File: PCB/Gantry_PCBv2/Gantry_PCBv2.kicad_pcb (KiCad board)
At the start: 2 copper layers, 190.5 x 121.8 mm, 169 parts, among them J1 Screw_Terminal_01x02, J10 B2B-XH-A_LF__SN_, J11 USB_C_Receptacle_USB2.0_16P, J12 Conn_01x04_Pin, J13 Conn_01x04_Pin, J14 Conn_01x04_Pin, J15 Conn_01x04_Pin, J16 Conn_01x05_Pin, J17 Conn_01x05_Pin, J2 DCJ200-10-A-XX-X_REVA, J3 Conn_01x03_Pin, J4 Conn_01x14, J5 B2B-XH-A_LF__SN_, J6 B2B-XH-A_LF__SN_, J7 B2B-XH-A_LF__SN_, J8 Conn_01x14, J9 Conn_01x10, Q1 NMOS, Q2 SS8050, Q3 SS8050, SW1 SW_0, SW2 SW_EN, SW3 SW_Push_DPDT, SW4 SW_Push_DPDT, SW5 SW_Push_DPDT, SW6 SW_Push_DPDT, U10 74HC245, U11 74HC245, U12 MCP23017_SO, U13 CP2102N-Axx-xQFN28, U14 ESP32-WROOM-32U, U2 MP1584, U4 TLV75733PDBV, U5 DRV8825_STEPPER_MOTOR_DRIVER_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, U6 DRV8825_STEPPER_MOTOR_DRIVER_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, U7 TB6612FNG H-bridge Motor Driv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, U8 DRV8825_STEPPER_MOTOR_DRIVER_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, U9 DRV8825_STEPPER_MOTOR_DRIVER_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

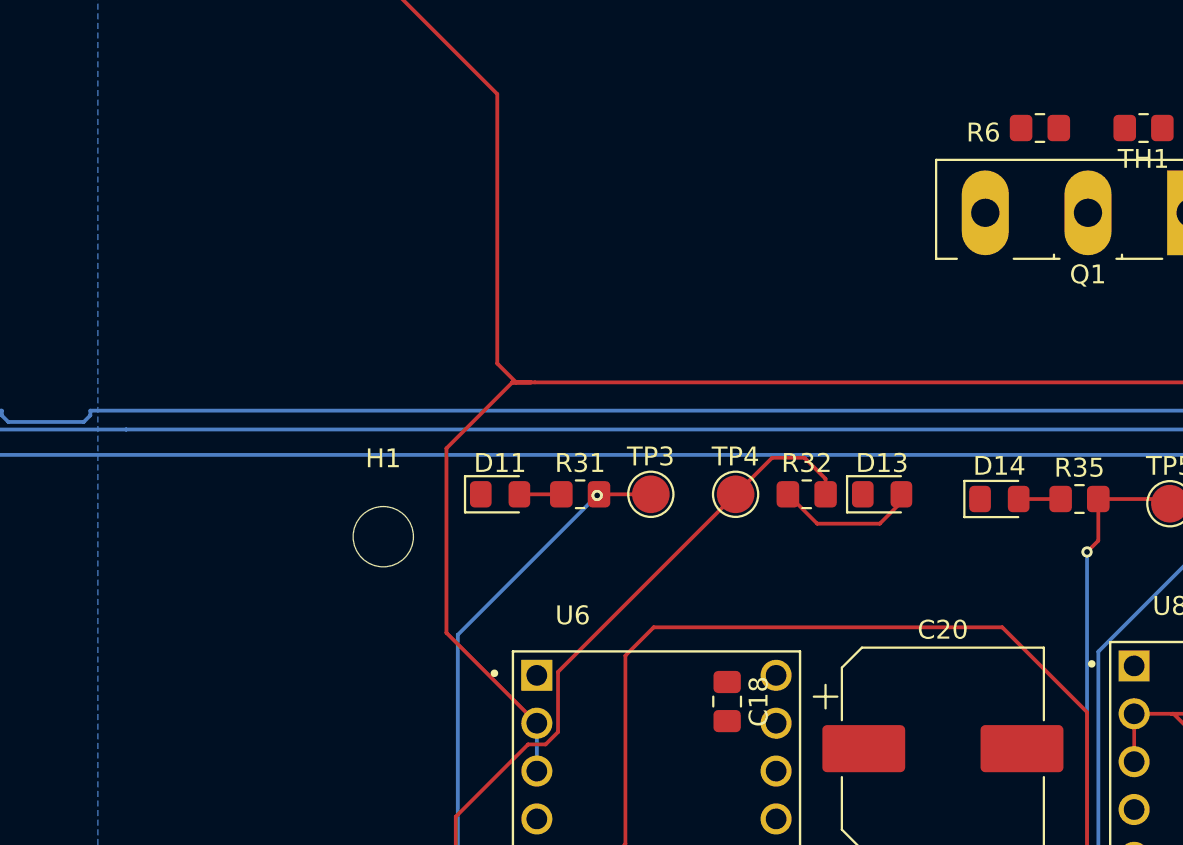
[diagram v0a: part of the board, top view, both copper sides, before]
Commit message: Changed footprint of potentiometer
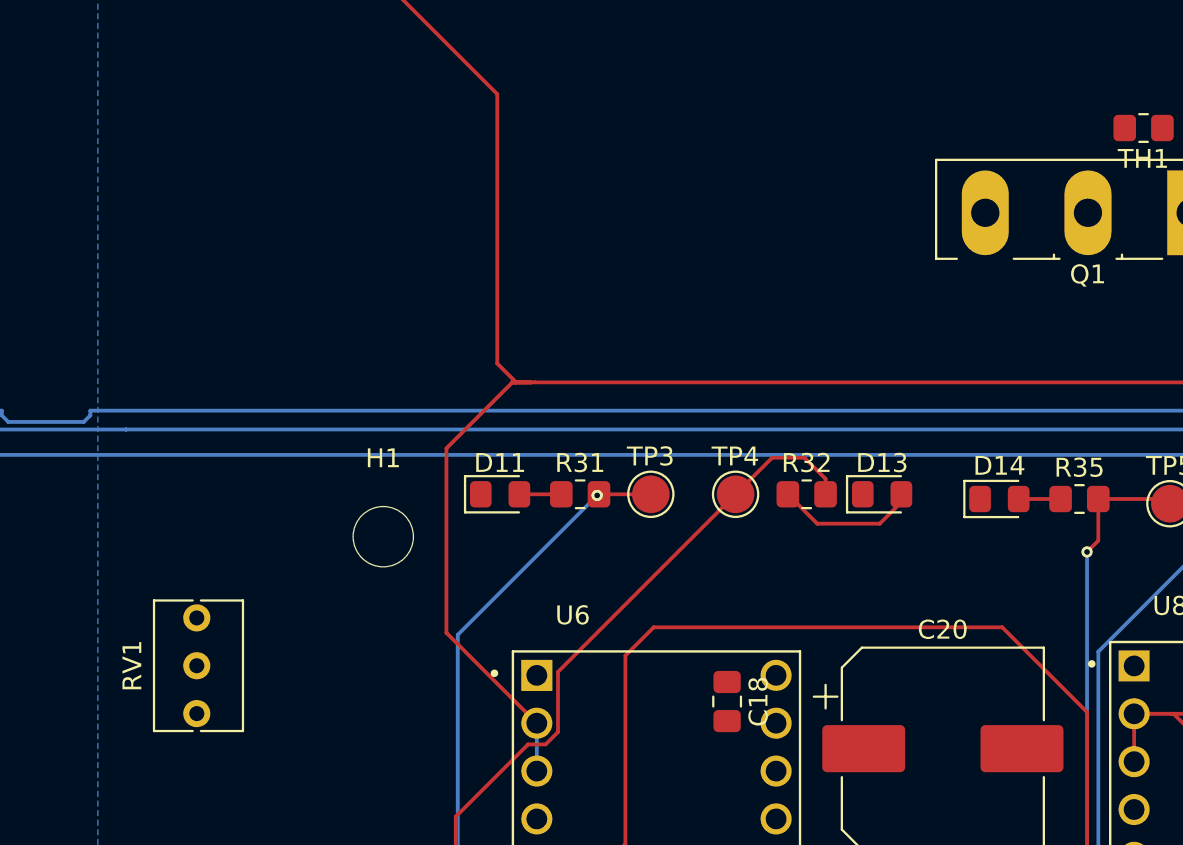
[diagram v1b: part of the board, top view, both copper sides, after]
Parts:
- removed R6: 10k, Resistor_SMD:R_0805_2012Metric_Pad1.20x1.40mm_HandSolder
- added RV1: Potentiometer, Potentiometer_THT:Potentiometer_Bourns_3266Y_Vertical, F.Cu at (150.0, 82.5)
- F1: value 3A -> 5A
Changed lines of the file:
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@@
 			)
 		)
-		(property "Value" "3A"
+		(property "Value" "5A"
 			(at 5.5 3.6 0)
 			(layer "F.Fab")
@@
 		)
 	)
+	(footprint "Potentiometer_THT:Potentiometer_Bourns_3266Y_Vertical"
+		(layer "F.Cu")
+		(at 150 82.5 90)
+		(descr "Potentiometer, vertical, Bourns 3266Y, https://www.bourns.com/docs/Product-Datasheets/3266.pdf")
+		(tags "Potentiometer vertical Bourns 3266Y")
+		(property "Reference" "RV1"
+			(at -2.54 -3.41 90)
+			(layer "F.SilkS")
+			(effects
+				(font
+					(size 1 1)
+					(thickness 0.15)
+				)
+			)
+		)
+		(property "Value" "Potentiometer"
+			(at -2.54 3.59 90)
+			(layer "F.Fab")
+			(effects
+				(font
+					(size 1 1)
+					(thickness 0.15)
+				)
+			)
+		)
+		(property "Datasheet" ""
+			(at 0 0 90)
+			(layer "F.Fab")
+			(hide yes)
+			(effects
+				(font
+					(size 1.27 1.27)
+					(thickness 0.15)
+				)
+			)
+		)
+		(property "Description" "Potentiometer"
+			(at 0 0 90)
+			(layer "F.Fab")
+			(hide yes)
+			(effects
+				(font
+					(size 1.27 1.27)
+					(thickness 0.15)
+				)
+			)
+		)
+		(property ki_fp_filters "Potentiometer*")
+		(sheetname "/")
+		(sheetfile "Gantry_PCBv2.kicad_sch")
+		(attr through_hole)
+		(fp_line
+			(start 0.925 -2.27)
+			(end 0.925 -0.217)
+			(stroke
+				(width 0.12)
+				(type solid)
+			)
+			(layer "F.SilkS")
+		)
+		(fp_line
+			(start -6.005 -2.27)
+			(end 0.925 -2.27)
+			(stroke
+				(width 0.12)
+				(type solid)
+			)
+			(layer "F.SilkS")
+		)
+		(fp_line
+			(start -6.005 -2.27)
+			(end -6.005 -0.217)
+			(stroke
+				(width 0.12)
+				(type solid)
+			)
+			(layer "F.SilkS")
+		)
+		(fp_line
+			(start 0.925 0.217)
+			(end 0.925 2.45)
+			(stroke
+				(width 0.12)
+				(type solid)
+			)
+			(layer "F.SilkS")
+		)
+		(fp_line
+			(start -6.005 0.217)
+			(end -6.005 2.45)
+			(stroke
+				(width 0.12)
+				(type solid)
+			)
+			(layer "F.SilkS")
+		)
+		(fp_line
+			(start -6.005 2.45)
+			(end 0.925 2.45)
+			(stroke
+				(width 0.12)
+				(type solid)
+			)
+			(layer "F.SilkS")
+		)
+		(fp_rect
+			(start -6.15 -2.41)
+			(end 1.07 2.59)
+			(stroke
+				(width 0.05)
+				(type solid)
+			)
+			(fill no)
+			(layer "F.CrtYd")
+		)
+		(fp_line
+			(start 0.161 0.395)
+			(end -1.08 1.636)
+			(stroke
+				(width 0.1)
+				(type solid)
+			)
+			(layer "F.Fab")
+		)
+		(fp_line
+			(start 0.27 0.504)
+			(end -0.971 1.745)
+			(stroke
+				(width 0.1)
+				(type solid)
+			)
+			(layer "F.Fab")
+		)
+		(fp_rect
+			(start -5.895 -2.16)
+			(end 0.815 2.34)
+			(stroke
+				(width 0.1)
+				(type solid)
+			)
+			(fill no)
+			(layer "F.Fab")
+		)
+		(fp_circle
+			(center -0.405 1.07)
+			(end 0.485 1.07)
+			(stroke
+				(width 0.1)
+				(type solid)
+			)
+			(fill no)
+			(layer "F.Fab")
+		)
+		(fp_text user "${REFERENCE}"
+			(at -3.15 0.09 90)
+			(layer "F.Fab")
+			(effects
+				(font
+					(size 0.92 0.92)
+					(thickness 0.14)
+				)
+			)
+		)
+		(pad "1" thru_hole circle
+			(at 0 0 90)
+			(size 1.44 1.44)
+			(drill 0.8)
+			(layers "*.Cu" "*.Mask")
+			(remove_unused_layers no)
+			(net 113 "Net-(Q1-G)")
+			(pinfunction "1")
+			(pintype "passive")
+		)
+		(pad "2" thru_hole circle
+			(at -2.54 0 90)
+			(size 1.44 1.44)
+			(drill 0.8)
+			(layers "*.Cu" "*.Mask")
+			(remove_unused_layers no)
+			(net 113 "Net-(Q1-G)")
+			(pinfunction "2")
+			(pintype "passive")
+		)
+		(pad "3" thru_hole circle
+			(at -5.08 0 90)
+			(size 1.44 1.44)
+			(drill 0.8)
+			(layers "*.Cu" "*.Mask")
+			(remove_unused_layers no)
+			(net 9 "/12V_P")
+			(pinfunction "3")
+			(pintype "passive")
+		)
+		(embedded_fonts no)
+		(model "${KICAD9_3DMODEL_DIR}/Potentiometer_THT.3dshapes/Potentiometer_Bourns_3266Y_Vertical.step"
+			(offset
+				(xyz 0 0 0)
+			)
+			(scale
+				(xyz 1 1 1)
+			)
+			(rotate
+				(xyz 0 0 0)
+			)
+		)
+	)
 	(footprint "Resistor_SMD:R_0805_2012Metric_Pad1.20x1.40mm_HandSolder"
 		(layer "F.Cu")
@@
 			)
 			(scale
-				(xyz 1 1 1)
-			)
-			(rotate
-				(xyz 0 0 0)
-			)
-		)
-	)
-	(footprint "Resistor_SMD:R_0805_2012Metric_Pad1.20x1.40mm_HandSolder"
-		(layer "F.Cu")
-		(at 194.75 56.5 180)
-		(descr "Resistor SMD 0805 (2012 Metric), square (rectangular) end terminal, IPC-7351 nominal with elongated pad for handsoldering. (Body size source: IPC-SM-782 page 72, https://www.pcb-3d.com/wordpress/wp-content/uploads/ipc-sm-782a_amendment_1_and_2.pdf), generated with kicad-footprint-generator")
-		(tags "resistor handsolder")
-		(property "Reference" "R6"
-			(at 3 -0.25 0)
-			(layer "F.SilkS")
-			(effects
-				(font
-					(size 1 1)
-					(thickness 0.15)
-				)
-			)
-		)
-		(property "Value" "10k"
-			(at 0 1.65 0)
-			(layer "F.Fab")
-			(effects
-				(font
-					(size 1 1)
-					(thickness 0.15)
-				)
-			)
-		)
-		(property "Datasheet" ""
-			(at 0 0 0)
-			(layer "F.Fab")
-			(hide yes)
-			(effects
-				(font
-					(size 1.27 1.27)
-					(thickness 0.15)
-				)
-			)
-		)
-		(property "Description" "Variable resistor"
-			(at 0 0 0)
-			(layer "F.Fab")
-			(hide yes)
-			(effects
-				(font
-					(size 1.27 1.27)
-					(thickness 0.15)
-				)
-			)
-		)
-		(property ki_fp_filters "R_*")
-		(sheetname "/")
-		(sheetfile "Gantry_PCBv2.kicad_sch")
-		(attr smd)
-		(fp_line
-			(start -0.227064 0.735)
-			(end 0.227064 0.735)
-			(stroke
-				(width 0.12)
-				(type solid)
-			)
-			(layer "F.SilkS")
-		)
-		(fp_line
-			(start -0.227064 -0.735)
-			(end 0.227064 -0.735)
-			(stroke
-				(width 0.12)
-				(type solid)
-			)
-			(layer "F.SilkS")
-		)
-		(fp_line
-			(start 1.85 0.95)
-			(end -1.85 0.95)
-			(stroke
-				(width 0.05)
-				(type solid)
-			)
-			(layer "F.CrtYd")
-		)
-		(fp_line
-			(start 1.85 -0.95)
-			(end 1.85 0.95)
-			(stroke
-				(width 0.05)
-				(type solid)
-			)
-			(layer "F.CrtYd")
-		)
-		(fp_line
-			(start -1.85 0.95)
-			(end -1.85 -0.95)
-			(stroke
-				(width 0.05)
-				(type solid)
-			)
-			(layer "F.CrtYd")
-		)
-		(fp_line
-			(start -1.85 -0.95)
-			(end 1.85 -0.95)
-			(stroke
-				(width 0.05)
-				(type solid)
-			)
-			(layer "F.CrtYd")
-		)
-		(fp_line
-			(start 1 0.625)
-			(end -1 0.625)
-			(stroke
-				(width 0.1)
-				(type solid)
-			)
-			(layer "F.Fab")
-		)
-		(fp_line
-			(start 1 -0.625)
-			(end 1 0.625)
-			(stroke
-				(width 0.1)
-				(type solid)
-			)
-			(layer "F.Fab")
-		)
-		(fp_line
-			(start -1 0.625)
-			(end -1 -0.625)
-			(stroke
-				(width 0.1)
-				(type solid)
-			)
-			(layer "F.Fab")
-		)
-		(fp_line
-			(start -1 -0.625)
-			(end 1 -0.625)
-			(stroke
-				(width 0.1)
-				(type solid)
-			)
-			(layer "F.Fab")
-		)
-		(fp_text user "${REFERENCE}"
-			(at 0 0 0)
-			(layer "F.Fab")
-			(effects
-				(font
-					(size 0.5 0.5)
-					(thickness 0.08)
-				)
-			)
-		)
-		(pad "1" smd roundrect
-			(at -1 0 180)
-			(size 1.2 1.4)
-			(layers "F.Cu" "F.Mask" "F.Paste")
-			(roundrect_rratio 0.208333)
-			(net 113 "Net-(Q1-G)")
-			(pintype "passive")
-		)
-		(pad "2" smd roundrect
-			(at 1 0 180)
-			(size 1.2 1.4)
-			(layers "F.Cu" "F.Mask" "F.Paste")
-			(roundrect_rratio 0.208333)
-			(net 1 "GND")
-			(pintype "passive")
-		)
-		(embedded_fonts no)
-		(model "${KICAD9_3DMODEL_DIR}/Resistor_SMD.3dshapes/R_0805_2012Metric.step"
-			(offset
-				(xyz 0 0 0)
-			)
-			(scale
